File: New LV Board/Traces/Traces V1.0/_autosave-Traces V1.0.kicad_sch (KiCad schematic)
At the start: 13 parts, among them J1 B15B-PH-K-S, J2 B15B-PH-K-S, J3 B15B-PH-K-S, J4 Conn_01x12, J5 VBATT +, J6 Conn_01x12, J7 Conn_01x12, J8 Vs

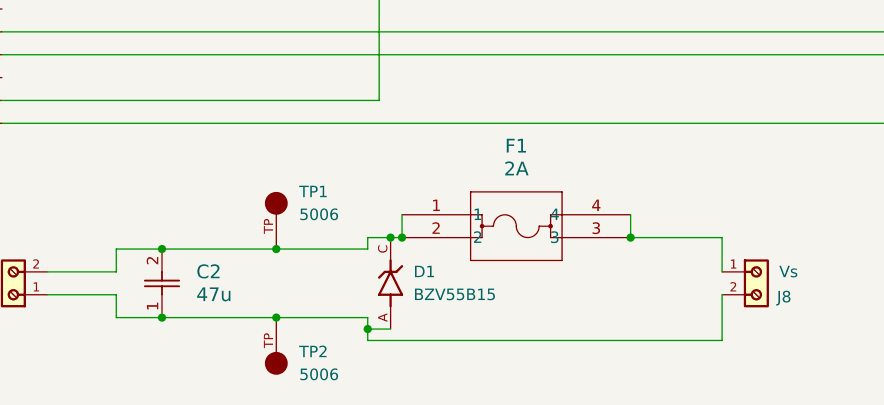
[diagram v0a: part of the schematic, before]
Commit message: changes to the traces files and added new components for the fuse and connector.
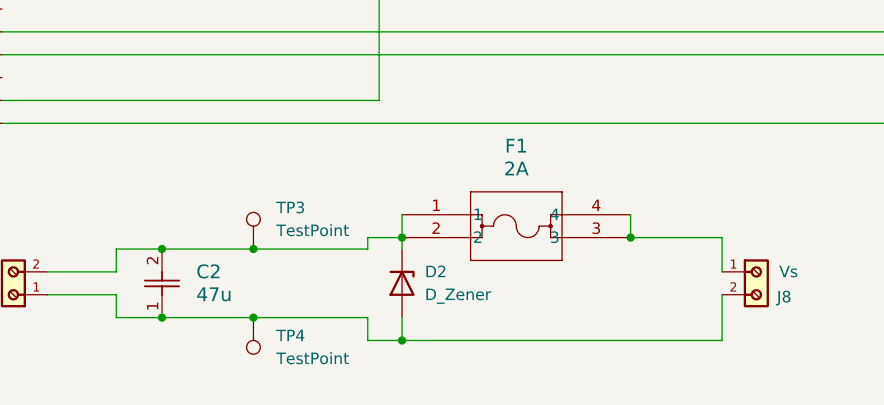
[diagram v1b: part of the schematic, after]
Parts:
- removed D1: BZV55B15, Diode_SMD:D_SC-80_HandSoldering, symbol BZV55B15:BZV55B15
- removed TP1, TP2: 5006, TestPoint:TestPoint_Keystone_5010-5014_Multipurpose, symbol 5006:5006
- added D2: D_Zener, Diode_SMD:D_1210_3225Metric, symbol Device:D_Zener
- added TP3, TP4: TestPoint, TestPoint:TestPoint_Keystone_5005-5009_Compact, symbol Connector:TestPoint
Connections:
- net at C2.1, J5.1, J8.2: now also D2.2 (A), TP4.1
- net at C2.2, F1.1, F1.2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: now also D2.1 (K), TP3.1
